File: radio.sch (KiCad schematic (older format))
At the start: 8 parts, among them U7 DRF1262x

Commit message: Add digikey pn's to schematic, update BOM
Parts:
- AE1: Digikey (none) -> CON-SMA-EDGE-S-ND
- C12, C14, U7: Digikey (none) -> DNP; LCSC (none) -> DNP
- C13: Digikey (none) -> 311-1439-1-ND
- C15: Digikey (none) -> 490-14603-1-ND
- L2: Digikey (none) -> 587-1932-1-ND
- L3: Digikey (none) -> 311-0.0JRCT-ND
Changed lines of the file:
@@
 F 2 "Custom_KICAD:DRF1262x" H 5350 3700 50  0001 C CNN
 F 3 "" H 5350 3700 50  0001 C CNN
-F 4 "" H 5350 3700 50  0001 C CNN "LCSC"
+F 4 "DNP" H 5350 3700 50  0001 C CNN "LCSC"
+F 5 "DNP" H 5350 3700 50  0001 C CNN "Digikey"
 	1    5350 3700
 	1    0    0    -1
@@
 F 3 "~" H 3650 3550 50  0001 C CNN
 F 4 "C1015" V 3650 3550 50  0001 C CNN "LCSC"
+F 5 "587-1932-1-ND" V 3650 3550 50  0001 C CNN "Digikey"
 	1    3650 3550
 	0    -1   -1   0
@@
 F 3 "~" H 4000 3800 50  0001 C CNN
 F 4 "C52923" H 4000 3800 50  0001 C CNN "LCSC"
+F 5 "311-1439-1-ND" H 4000 3800 50  0001 C CNN "Digikey"
 	1    4000 3800
 	1    0    0    -1
@@
 F 3 "~" H 4400 3800 50  0001 C CNN
 F 4 "C1525" H 4400 3800 50  0001 C CNN "LCSC"
+F 5 "490-14603-1-ND" H 4400 3800 50  0001 C CNN "Digikey"
 	1    4400 3800
 	1    0    0    -1
@@
 F 2 "jlcpcb_smt:C_0402_1005Metric" H 4188 1900 50  0001 C CNN
 F 3 "~" H 4150 2050 50  0001 C CNN
+F 4 "DNP" H 4150 2050 50  0001 C CNN "LCSC"
+F 5 "DNP" H 4150 2050 50  0001 C CNN "Digikey"
 	1    4150 2050
 	1    0    0    -1
@@
 F 2 "jlcpcb_smt:R_0402_1005Metric" H 3338 1900 50  0001 C CNN
 F 3 "~" H 3300 2050 50  0001 C CNN
+F 4 "DNP" H 3300 2050 50  0001 C CNN "LCSC"
+F 5 "DNP" H 3300 2050 50  0001 C CNN "Digikey"
 	1    3300 2050
 	1    0    0    -1
@@
 F 3 "~" H 3750 1750 50  0001 C CNN
 F 4 "C17168" V 3750 1750 50  0001 C CNN "LCSC"
+F 5 "311-0.0JRCT-ND" V 3750 1750 50  0001 C CNN "Digikey"
 	1    3750 1750
 	0    -1   -1   0
@@
 F 3 "~" H 2900 1600 50  0001 C CNN
 F 4 "C129604" H 2900 1500 50  0001 C CNN "LCSC"
+F 5 "CON-SMA-EDGE-S-ND" H 2900 1500 50  0001 C CNN "Digikey"
 	1    2900 1500
 	-1   0    0    -1
@@
 	5800 3950 6050 3950
 $Comp
-L Graphic:Logo_Open_Hardware_Small #LOGO?
+L Graphic:Logo_Open_Hardware_Small #LOGO4
 U 1 1 5DD37E60
 P 10750 6850
-F 0 "#LOGO?" H 10750 7125 50  0001 C CNN
+F 0 "#LOGO4" H 10750 7125 50  0001 C CNN
 F 1 "Logo_Open_Hardware_Small" H 10750 6625 50  0001 C CNN
 F 2 "" H 10750 6850 50  0001 C CNN
@@
 $EndComp
 $Comp
-L Graphic:SYM_Radio_Waves_Large #SYM?
+L Graphic:SYM_Radio_Waves_Large #SYM4
 U 1 1 5DD37E66
 P 10200 6800
-F 0 "#SYM?" H 10200 7000 50  0001 C CNN
+F 0 "#SYM4" H 10200 7000 50  0001 C CNN
 F 1 "SYM_Radio_Waves_Large" H 10200 6550 50  0001 C CNN
 F 2 "" H 10200 6600 50  0001 C CNN

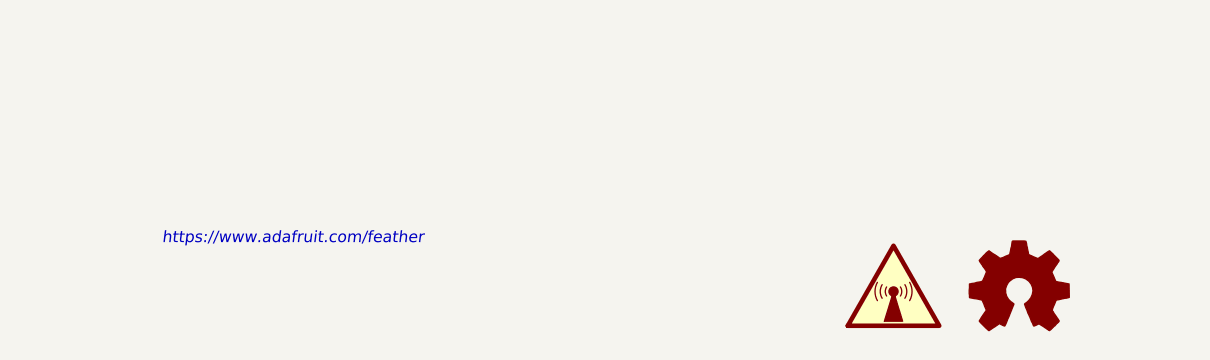
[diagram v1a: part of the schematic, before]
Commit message: PCB REV C0 * Make U8 footprint capable of crypto and fram device * Minor updates to schematic * Minor updates to doc prints * Update bot silk to REV C0
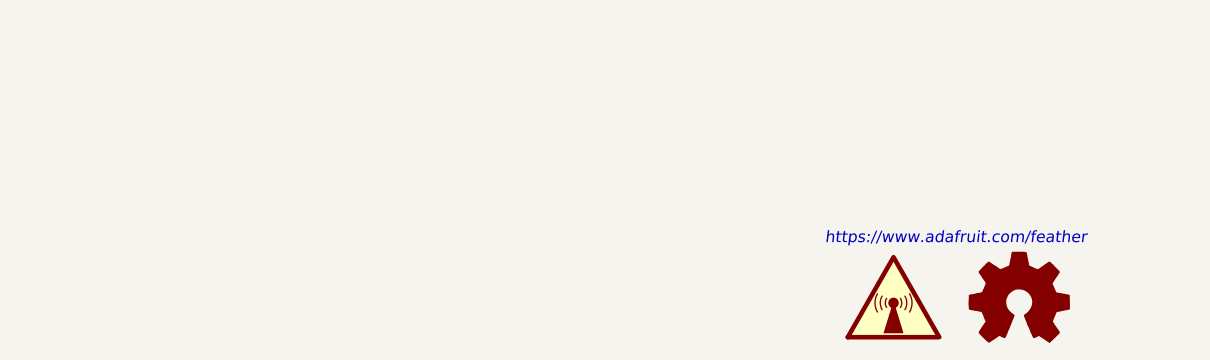
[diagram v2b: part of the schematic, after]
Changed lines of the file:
@@
 L Graphic:Logo_Open_Hardware_Small #LOGO4
 U 1 1 5DD37E60
-P 10750 6850
-F 0 "#LOGO4" H 10750 7125 50  0001 C CNN
-F 1 "Logo_Open_Hardware_Small" H 10750 6625 50  0001 C CNN
-F 2 "" H 10750 6850 50  0001 C CNN
-F 3 "~" H 10750 6850 50  0001 C CNN
-	1    10750 6850
+P 10750 6900
+F 0 "#LOGO4" H 10750 7175 50  0001 C CNN
+F 1 "Logo_Open_Hardware_Small" H 10750 6675 50  0001 C CNN
+F 2 "" H 10750 6900 50  0001 C CNN
+F 3 "~" H 10750 6900 50  0001 C CNN
+	1    10750 6900
 	1    0    0    -1
 $EndComp
@@
 L Graphic:SYM_Radio_Waves_Large #SYM4
 U 1 1 5DD37E66
-P 10200 6800
-F 0 "#SYM4" H 10200 7000 50  0001 C CNN
-F 1 "SYM_Radio_Waves_Large" H 10200 6550 50  0001 C CNN
-F 2 "" H 10200 6600 50  0001 C CNN
-F 3 "~" H 10230 6600 50  0001 C CNN
-	1    10200 6800
+P 10200 6850
+F 0 "#SYM4" H 10200 7050 50  0001 C CNN
+F 1 "SYM_Radio_Waves_Large" H 10200 6600 50  0001 C CNN
+F 2 "" H 10200 6650 50  0001 C CNN
+F 3 "~" H 10230 6650 50  0001 C CNN
+	1    10200 6850
 	1    0    0    -1
 $EndComp
@@
 EndData
 $EndBitmap
-Text Notes 7000 6650 0    50   Italic 0
+Text Notes 9900 6650 0    50   Italic 0
 https://www.adafruit.com/feather
 $Bitmap
